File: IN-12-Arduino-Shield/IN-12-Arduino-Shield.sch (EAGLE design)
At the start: 21 parts, among them T1 IN-12, T2 IN-12, T3 IN-12, T4 IN-12, U1 K155ID1, U2 K155ID1, U3 K155ID1, U4 K155ID1, U5 ARDUINOR3-DIMENSION

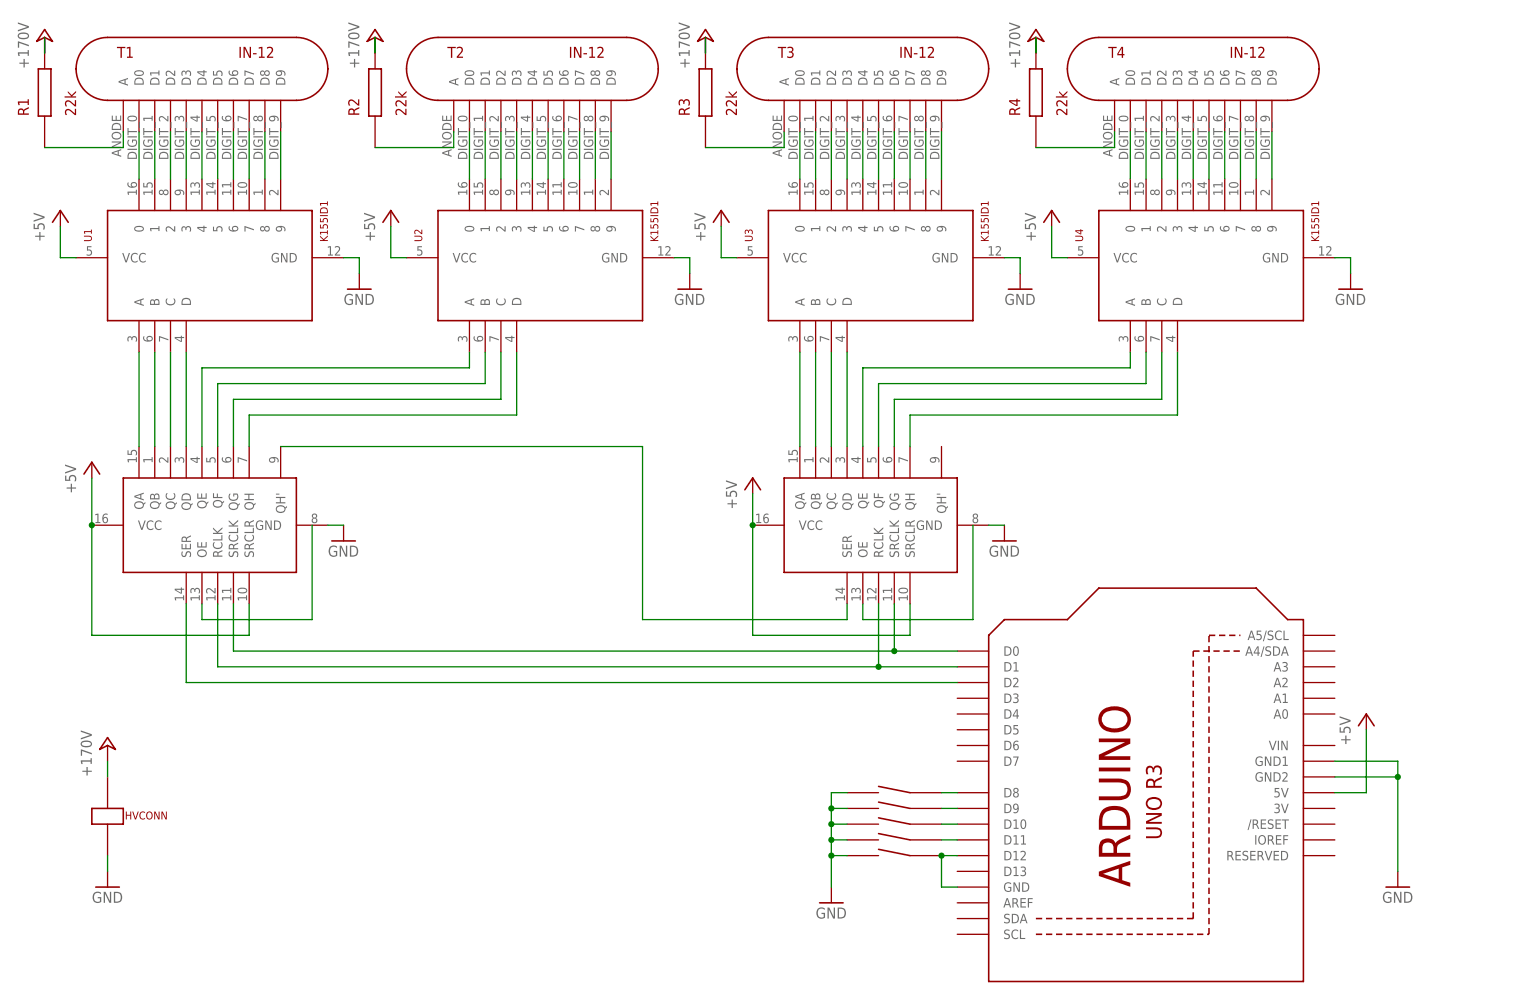
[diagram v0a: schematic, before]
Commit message: Fixed tube orientation. Added firmware example code.
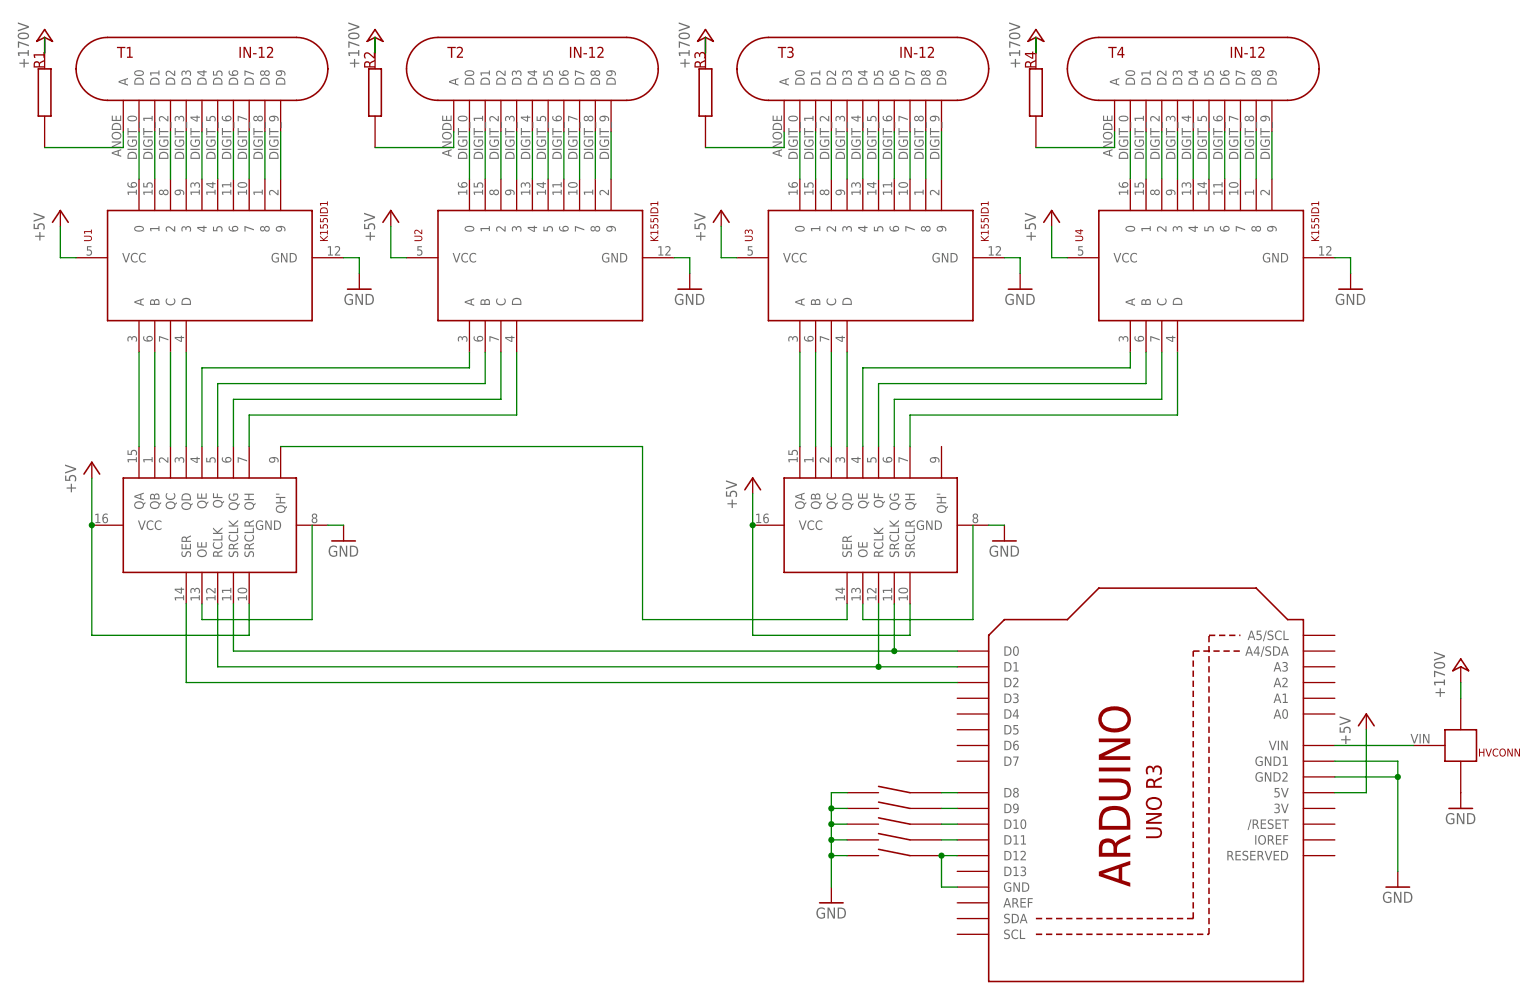
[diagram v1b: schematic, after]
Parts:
- R1, R2, R3, R4: value 22k -> 5,6K
- U5: value ARDUINOR3-DIMENSION -> ARDUINOR3; device TimeExpander:ARDUINOR3-DIMENSION -> TimeExpander:ARDUINOR3
- renumbered U$1 to U6, U$2 to U7
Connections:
- new net N$55: HVCONN.VIN, U5.VIN
